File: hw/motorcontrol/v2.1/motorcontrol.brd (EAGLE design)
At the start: 65 x 57.2 mm, 117 parts, among them U1 BTN8982TA, U10 SN74LV4T125, U11 SI2333CDS-T1-GE3, U12 BSS138BKS, U13 BSS138BKS, U2 BTN8982TA, U3 BTN8982TA, U4 CAT24C32, U5 SN74LV4T125, U6 MMDT5401, U7 PTR08060W, U8 IPD90P03P4L-04, U9 ATMEGA32U4

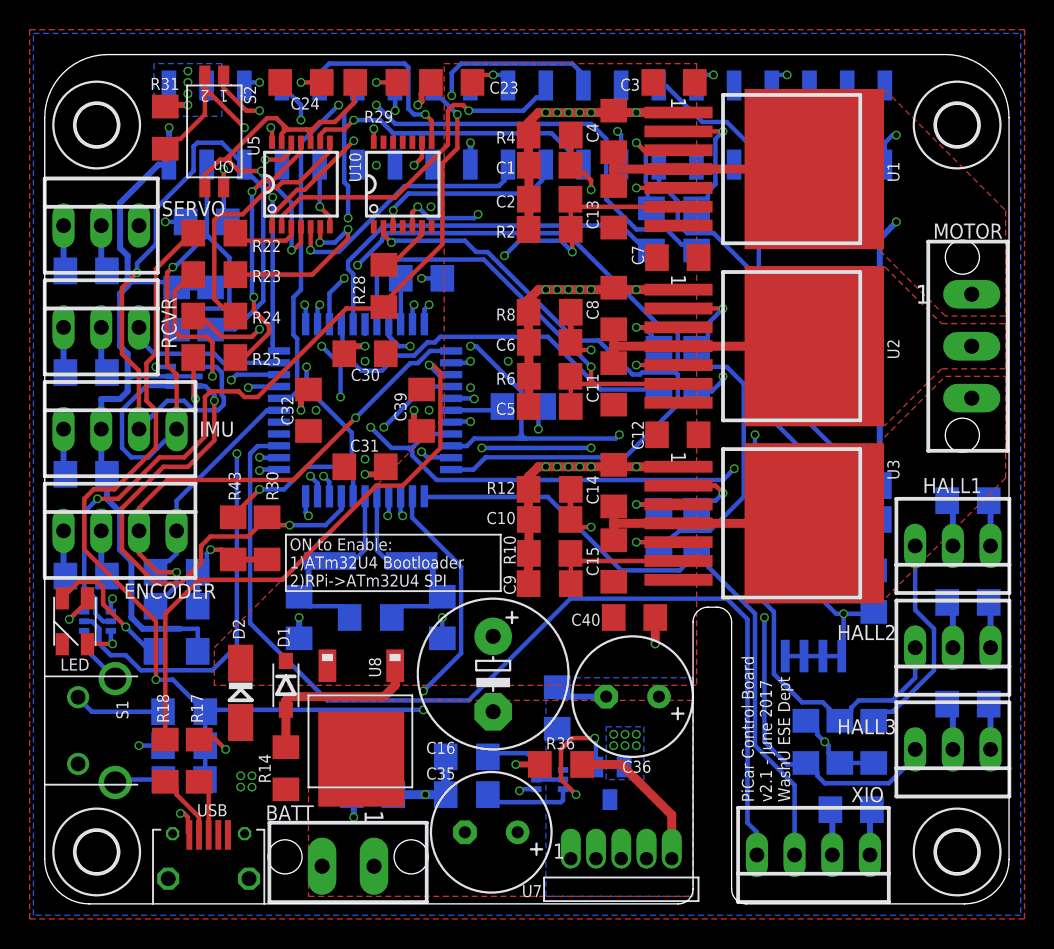
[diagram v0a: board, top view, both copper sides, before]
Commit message: fixed error in connection between IS U3 and ATADC4
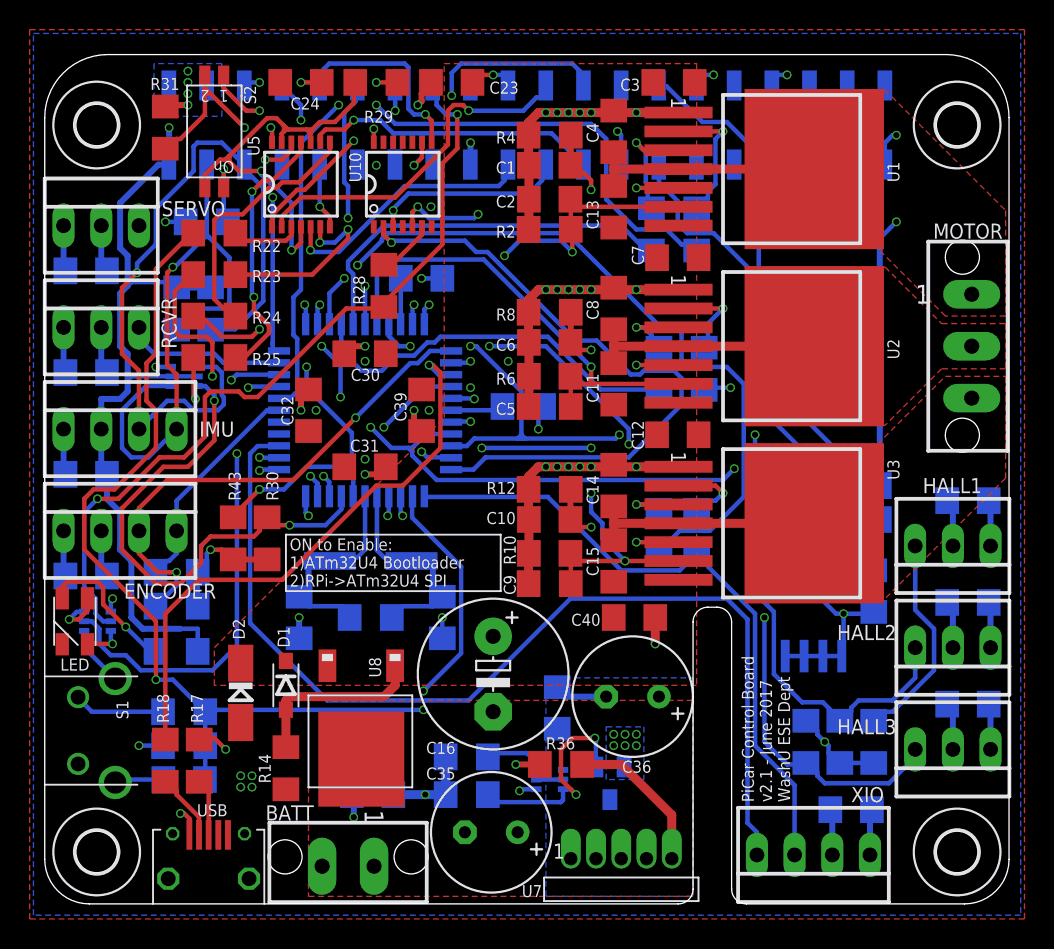
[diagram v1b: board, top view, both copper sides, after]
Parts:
- moved R7 0.51 mm to (44.5, 36.1)
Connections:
- removed net ATADC2: C9.1, R10.2, U3.6
- removed net ATPD6: U9.26
- removed net ATPD7: U9.27
- net ATADC4: now also C9.1, R10.2, U3.6
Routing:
- net ATADC4: track 0.66 -> 45.1 mm, vias 0 -> 5
- net ATADC2: track 9.90 -> 0.00 mm
- net RPIGND: track 33.2 -> 32.4 mm
- net RPILEDB: track 53.9 -> 54.4 mm
